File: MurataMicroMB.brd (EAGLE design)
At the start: 160 x 100 mm, 10 parts, among them CON1 CON_MICROSD_C2395, CON3 CON_MIL_10_ARM, IC1 74LVC1G00DBV

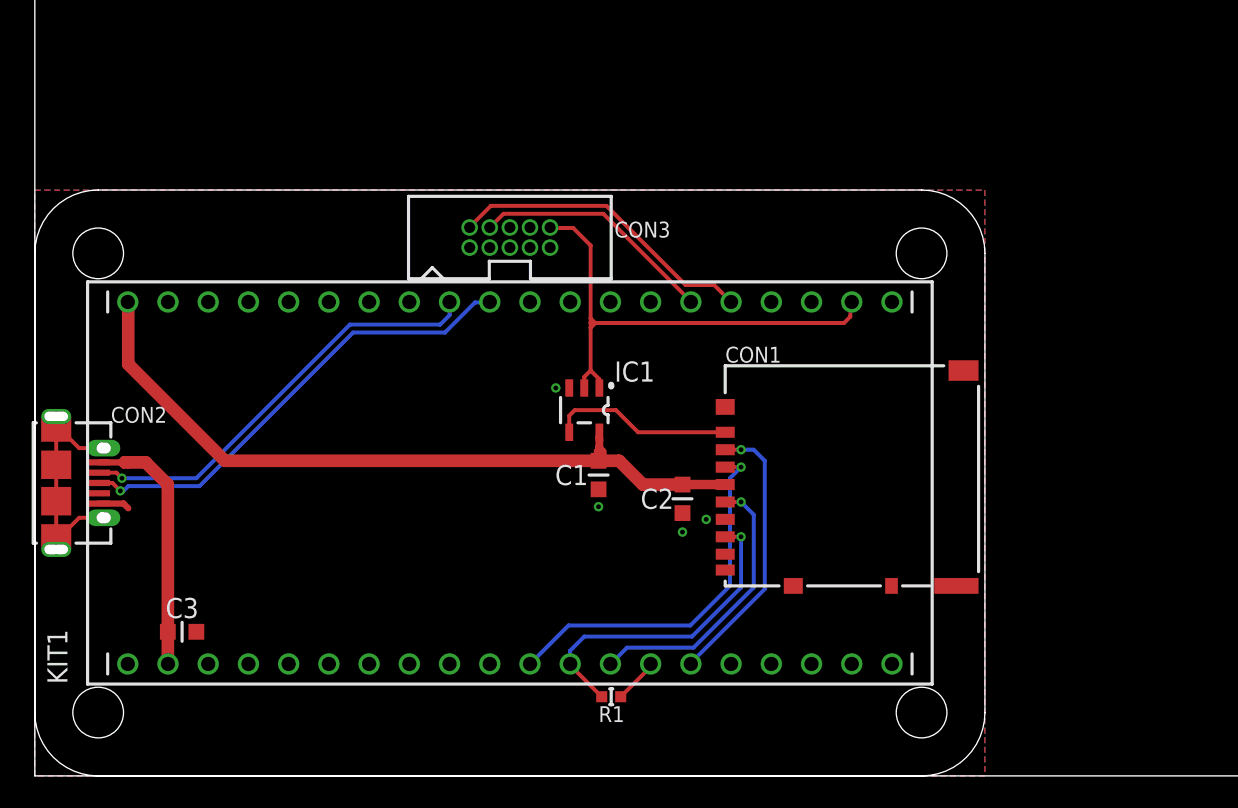
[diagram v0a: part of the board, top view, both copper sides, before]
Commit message: [ FIX ] add DCDC converter(for Vpp), microSD sockets, switches, USB circuit
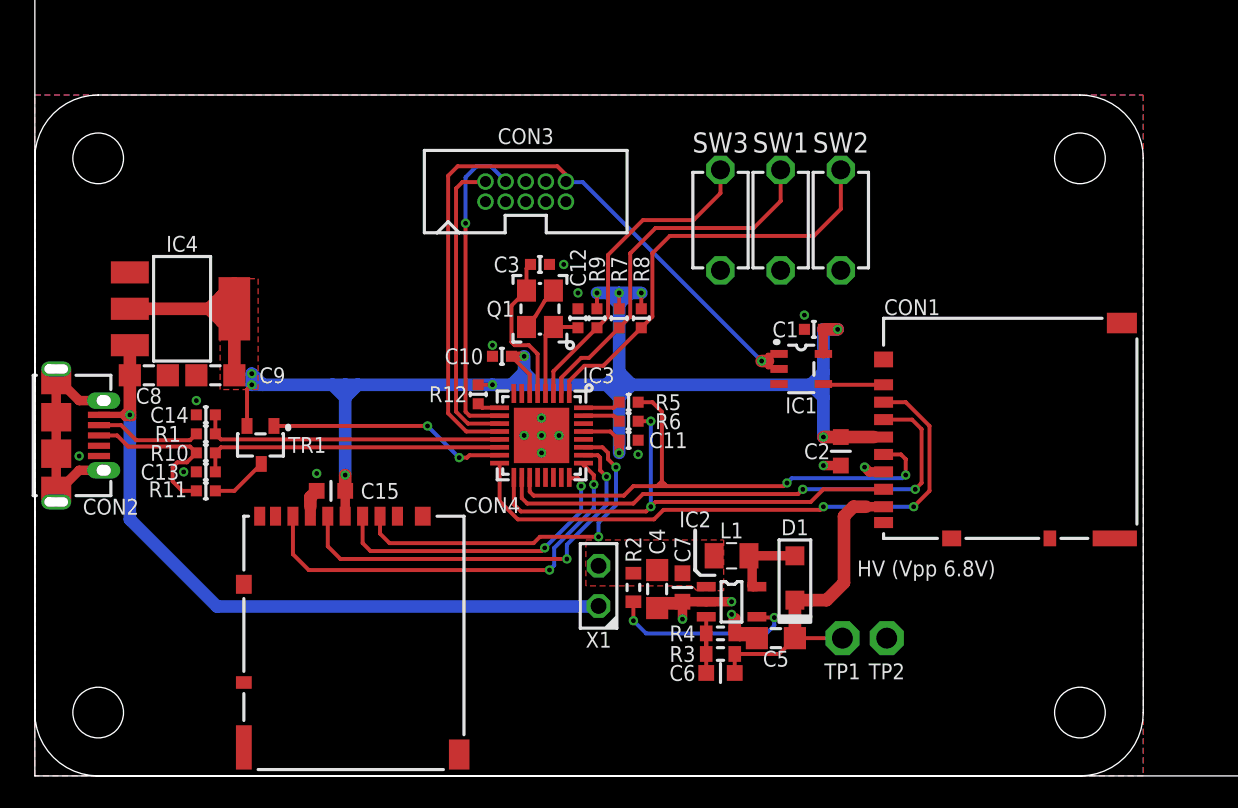
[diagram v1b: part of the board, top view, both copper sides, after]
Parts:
- removed KIT1: MBED_NXP_LPC1768, MBED_v2.1:MBED-KIT
- added C10, C11, C12: 4.7u, mylib:C0402
- added C13, C14: 18p/1005, mylib:C0402
- added C15, C6: (no value), mylib:CR_1608
- added C4, C5, C8, C9: 4.7u, mylib:CR_2125
- added C7: 0.1u, mylib:CR_1608
- added CON4: CON_MICROSD_C2395, mylib:CON_MICROSD_C2395
- added D1: DIODE_SMALL, mylib:DIODE_2125
- added IC2: IC_DCDC_LM27313, mylib:IC_05_0.95_50MIL
- added IC3: IC_LPC11U3XQFN33, mylib:HVQFN33
- added IC4: IC_LDO_XX1117_4, mylib:IC_SOT223
- added L1: 4.7u, mylib:L_2016
- added Q1: CLOCK_CRYSTAL_4_3225, mylib:CLOCK_3225
- added R10: 33/1005, mylib:C0402
- added R11: 1.5k/1005, mylib:C0402
- added R12, R5, R6, R7, R8, R9: (no value), mylib:C0402
- added R2: 10k, mylib:R_1608_PADPAD
- added R3: 60.4k, mylib:R_1608_PADPAD
- added R4: 13.3k, mylib:R_1608_PADPAD
- added SW1, SW2, SW3: SW_TACTSW_2PP8073, mylib:SW_TACTSW_P8073
- added TP1, TP2: TPPAD1-13, testpad_local:P1-13
- added TR1: I-4269, mylib:SOT95P300X140-3N
- added X1: TSW-102-02-S-S, con-samtec.local:TSW-102-02-S-S
- C1: device mylib:CR_1608 -> mylib:C0402
- C3: value (none) -> 4.7u; device mylib:CR_1608 -> mylib:C0402
- PCB1: value PCB_DP_RECTANGLE-37X60 -> PCB_DP_RECTANGLE-43X70; device dp_pcb:DP6037_V1 -> dp_pcb:DP7043_V1
- R1: value (none) -> 33/1005
- moved C3 32.4 mm to (31.9, 32.3)
- moved R1 30.5 mm to (10.8, 21.6)
- moved C1 16.4 mm to (49.2, 28.2), turned to 180 degrees
- moved IC1 13.9 mm to (48.4, 25.7), turned to 270 degrees
- moved C2 10.4 mm to (50.9, 20.5)
- moved CON1 10.4 mm to (69.6, 21.5)
- moved PCB1 5.83 mm to (35.0, 21.5)
- moved CON3 3.07 mm to (31.0, 36.9)
- moved CON2 3.00 mm to (-0.10, 21.5)
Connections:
- removed net N$1: CON2.2, KIT1.D-
- removed net NR: KIT1.NR
- removed net VB: KIT1.VB
- removed net VU: KIT1.VU
- new net !RESET!: IC3.2, R7.2, SW1.A2
- new net BL: IC3.1, R8.2, SW2.A2
- new net CS2: CON4.DAT3/CD, IC3.27
- new net D+: CON2.3, R10.1, R11.2
- new net D-: CON2.2, R1.1
- new net ISP: IC3.3, R9.2, SW3.A2
- new net MISO2: CON4.DAT0, IC3.25
- new net MOSI2: CON4.CMD, IC3.24
- new net N$10: C6.2, IC2.3, R3.1, R4.2
- new net N$11: C3.1, IC3.5, Q1.3
- new net N$12: IC3.15, TR1.1
- new net N$13: IC3.9, R12.2
- new net N$20: C13.1, IC3.14, R10.2
- new net N$24: C14.1, IC3.13, R1.2
- new net N$6: IC3.31, R6.1
- new net N$7: D1.A, IC2.5, L1.2
- new net N$8: IC2.4, R2.1
- new net N$9: IC3.32, R5.1
- new net SCK2: CON4.CLK, IC3.26
- new net VIN: C4.1, C7.1, IC2.1, L1.1, R2.2, X1.2
- net !CS!: now also IC3.16; no longer KIT1.P$15
- net 3.3V: now also C10.1, C11.1, C15.1, C9.1, CON4.VDD, IC3.29, IC3.6, IC4.2, IC4.4, R12.1, R7.1, R8.1, R9.1, TR1.2; no longer KIT1.VOUT
- net GND: now also C10.2, C11.2, C12.2, C13.2, C14.2, C15.2, C4.2, C5.2, C7.2, C8.2, C9.2, CON4.SHLD, CON4.SHLD@2, CON4.SHLD@3, CON4.SHLD@4, CON4.VSS, IC2.2, IC3.EXP, IC4.1, Q1.2, Q1.4, R4.1, SW1.A1, SW2.A1, SW3.A1, TP2.TP; no longer KIT1.GND
- net MISO: now also IC3.17, R6.2; no longer KIT1.P$12, R1.1
- net MOSI: now also IC3.18; no longer KIT1.P$11
- net N$2: now also R11.1, TR1.3; no longer CON2.3, KIT1.D+
- net N$5: now also C12.1, IC3.4, Q1.1; no longer KIT1.P$14, R1.2
- net NSRST: now also IC3.12; no longer KIT1.P$22
- net SCK: now also IC3.19, R5.2; no longer KIT1.P$13
- net SWCLK: now also IC3.10; no longer KIT1.P$26
- net SWDIO: now also IC3.11; no longer KIT1.P$25
- net VBUS: now also C8.1, IC4.3, X1.1; no longer C3.1, KIT1.VIN
- net VPP: now also C5.1, C6.1, D1.K, R3.2, TP1.TP
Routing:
- net 3.3V: track 50.0 -> 121.7 mm, vias 0 -> 11
- net VBUS: track 17.8 -> 47.2 mm, vias 0 -> 1
- net N$1: track 27.4 -> 0.00 mm, vias 1 -> 0
- net BL: track 0.00 -> 27.3 mm
- net MISO2: track 0.00 -> 27.2 mm, vias 0 -> 2
- net N$2: track 29.8 -> 3.60 mm, vias 1 -> 0
- net SCK2: track 0.00 -> 26.0 mm, vias 0 -> 2
- net !RESET!: track 0.00 -> 23.8 mm
- net CS2: track 0.00 -> 23.0 mm, vias 0 -> 2
- net VPP: track 0.00 -> 21.3 mm
- net !CS!: track 17.6 -> 38.4 mm, vias 1 -> 2
- net ISP: track 0.00 -> 20.4 mm
- net MOSI2: track 0.00 -> 19.5 mm, vias 0 -> 2
- net N$24: track 0.00 -> 19.3 mm
- net N$20: track 0.00 -> 19.3 mm
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- added copper zone on layer 1, net 3.3V
- added copper zone on layer 1, net VIN
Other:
- board text added: "HV (Vpp 6.8V)"

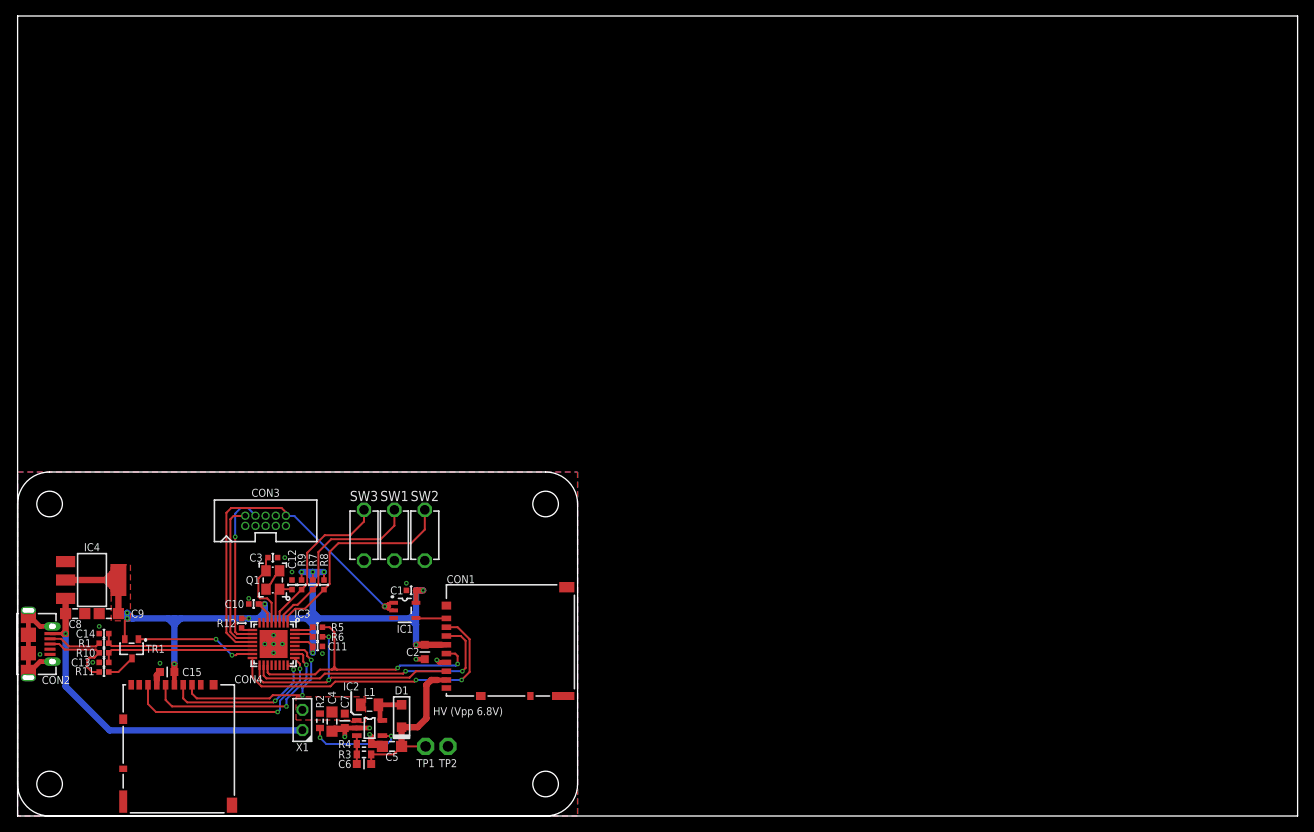
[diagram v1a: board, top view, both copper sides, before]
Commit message: [ MB ][ SCH ] R/C/L values
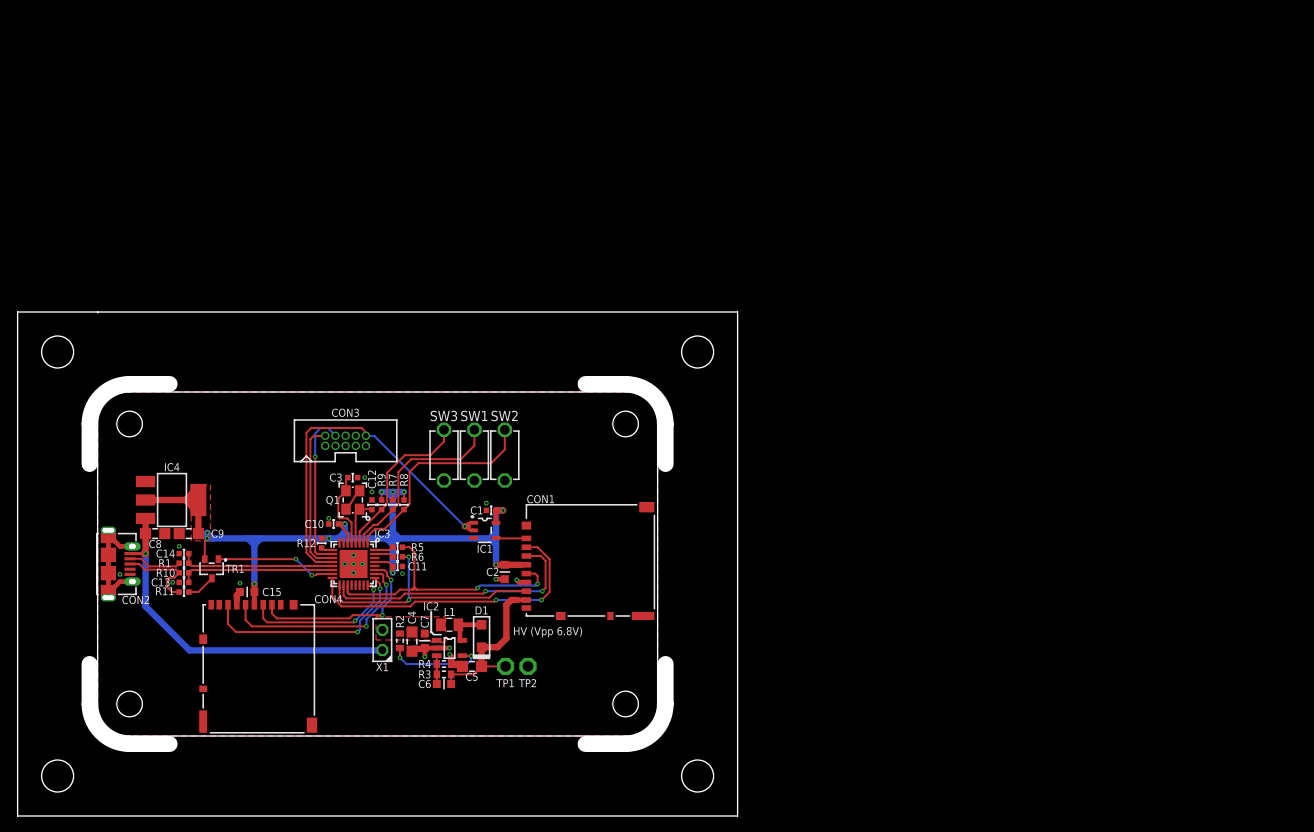
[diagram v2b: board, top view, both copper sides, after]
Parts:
- C1, C15, C2: value (none) -> 0.1u
- C10, C11: value 4.7u -> 0.1u
- C12, C3: value 4.7u -> 18p
- C6: value (none) -> NM
- CON1: value CON_MICROSD_C2395 -> C-2395.MurataMicroSD
- CON4: value CON_MICROSD_C2395 -> C-2395.microSD
- L1: value 4.7u -> 4.7uH/2016
- R12, R7, R8, R9: value (none) -> 10k
- R5, R6: value (none) -> 100
- moved C1 14.1 mm to (59.2, 38.2)
- moved IC1 14.1 mm to (58.4, 35.7)
- moved C10 14.1 mm to (39.5, 36.5)
- moved C11 14.1 mm to (47.5, 31.2)
- moved C12 14.1 mm to (44.3, 38.9)
- moved C13 14.1 mm to (20.8, 29.2)
- moved C15 14.1 mm to (28.7, 28.0)
- moved C2 14.1 mm to (60.9, 30.5)
- moved C3 14.1 mm to (41.9, 42.3)
- moved C4 14.1 mm to (49.3, 21.8)
- moved C5 14.1 mm to (56.8, 18.7)
- moved C6 14.1 mm to (53.3, 16.5)
- moved CON1 14.1 mm to (79.6, 31.5)
- moved CON2 14.1 mm to (9.90, 31.5)
- moved CON3 14.1 mm to (41.0, 46.9)
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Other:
- board size 160 x 100 mm -> 90 x 63 mm

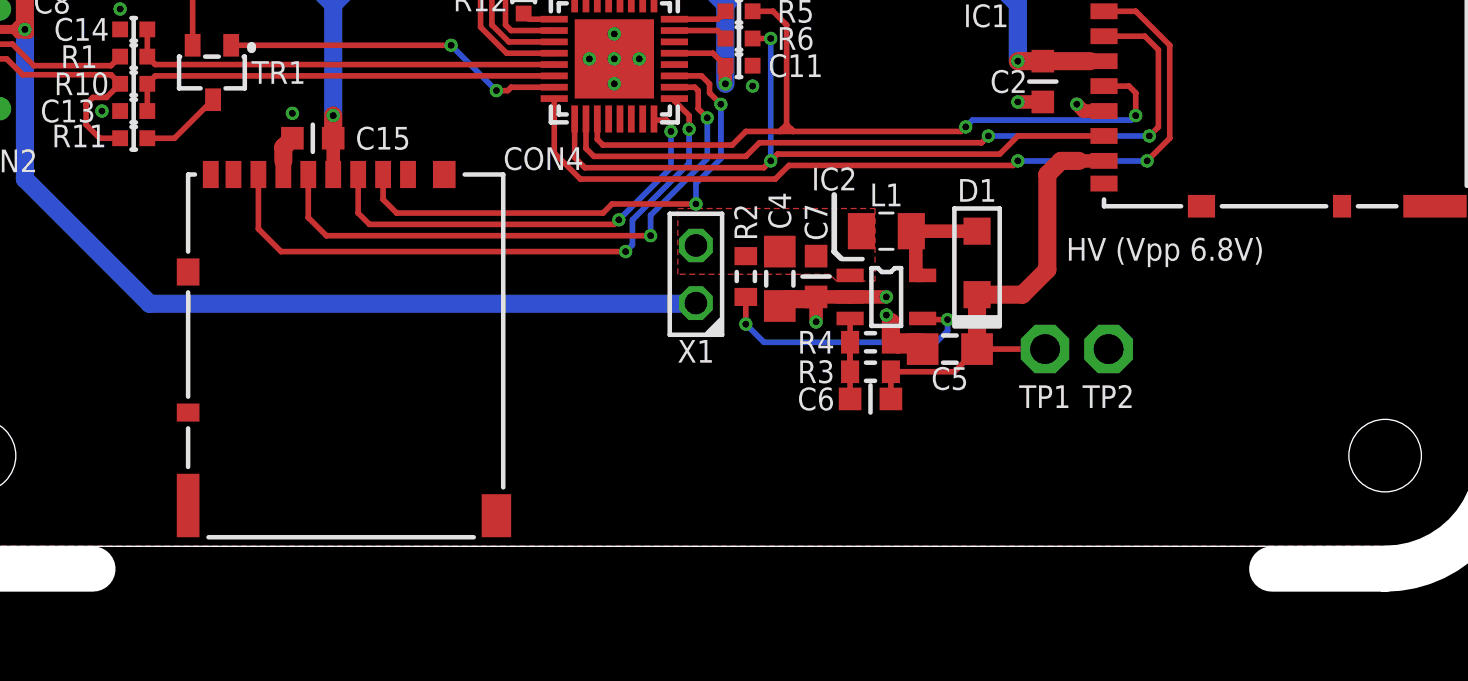
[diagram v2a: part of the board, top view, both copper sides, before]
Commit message: [ MB ] add OSHW icon
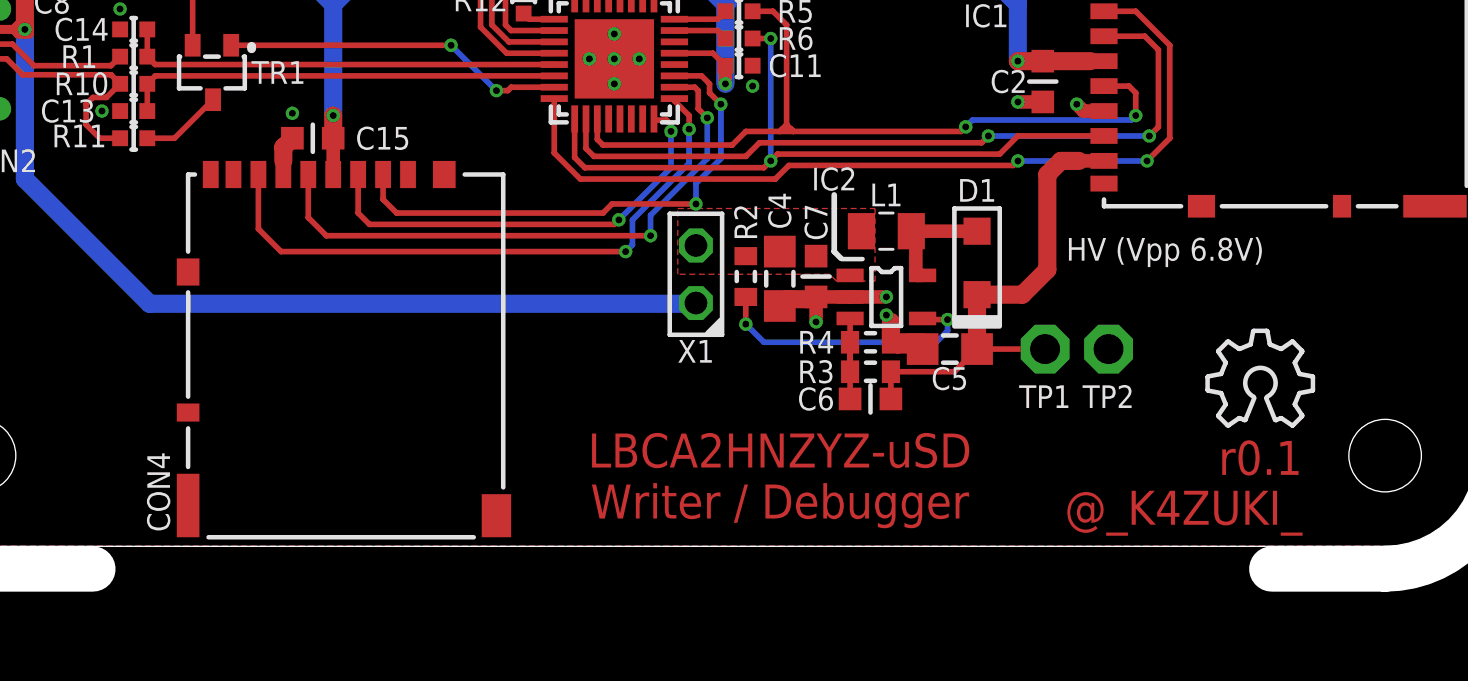
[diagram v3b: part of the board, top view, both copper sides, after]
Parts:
- added U$1: ICON_OSHW, mylib:ICON_OSHW
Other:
- board text added: "@_K4ZUKI_"
- board text added: "LBCA2HNZYZ-uSD Writer / Debugger"
- board text added: "r0.1"
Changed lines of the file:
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@@
 <wire x1="81" y1="19" x2="81" y2="14" width="2" layer="46"/>
 <wire x1="71" y1="9" x2="76" y2="9" width="2" layer="46"/>
+<text x="49.3" y="13.1" size="1.5" layer="1" ratio="20" align="center">LBCA2HNZYZ-uSD
+Writer / Debugger</text>
+<text x="70.5" y="13.9" size="1.5" layer="1" ratio="20" align="center">r0.1</text>
+<text x="67.1" y="11.7" size="1.5" layer="1" ratio="20" align="center">@_K4ZUKI_</text>
 </plain>
 <attributes>
@@
 <attribute name="VALUE" x="57.1" y="42.6" size="1.27" layer="27" font="vector" ratio="16" rot="R90"/>
 </element>
-<element name="CON4" library="mylib" package="CON_MICROSD_C2395" value="C-2395.microSD" x="29.7" y="10.4"/>
+<element name="CON4" library="mylib" package="CON_MICROSD_C2395" value="C-2395.microSD" x="29.7" y="10.4" smashed="yes">
+<attribute name="NAME" x="21.9" y="12.4" size="1" layer="25" ratio="20" rot="R90" align="center"/>
+</element>
 <element name="C15" library="mylib" package="CR_1608" value="0.1u" x="28.7" y="28" smashed="yes" rot="R180">
 <attribute name="NAME" x="31.8" y="28" size="1" layer="25" font="vector" ratio="20" rot="R180" align="center"/>
 <attribute name="VALUE" x="28.8" y="29.5" size="1.27" layer="27" font="vector" ratio="15" rot="R180" align="center"/>
 </element>
+<element name="U$1" library="mylib" package="ICON_OSHW" value="ICON_OSHW" x="70.5" y="17.2"/>
 </elements>
 <signals>
@@
 </board>
 </drawing>
+<compatibility>
+<note version="6.3" minversion="6.2.2" severity="warning">
+Since Version 6.2.2 text objects can contain more than one line,
+which will not be processed correctly with this version.
+</note>
+</compatibility>
 </eagle>
